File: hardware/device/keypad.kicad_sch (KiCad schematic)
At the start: 55 parts, among them SW1 TRIG1, SW10 TRIG10, SW11 TRIG11, SW12 TRIG12, SW13 TRIG13, SW14 TRIG14, SW15 TRIG15, SW16 TRIG16, SW17 WHEEL_BTN, SW18 HELP, SW19 LEFT_BTN, SW2 TRIG2, SW20 RIGHT_BTN, SW3 TRIG3, SW4 TRIG4, SW5 TRIG5, SW6 TRIG6, SW7 TRIG7, SW8 TRIG8, SW9 TRIG9, U10 TRIG9, U11 TRIG13, U12 TRIG10, U13 TRIG14, U14 TRIG11, U15 TRIG15, U16 TRIG12, U17 TRIG16, U2 TRIG1, U25 TCA8418RTWR, U3 TRIG2, U4 TRIG3, U5 TRIG4, U6 TRIG8, U7 TRIG7, U8 TRIG6, U9 TRIG5

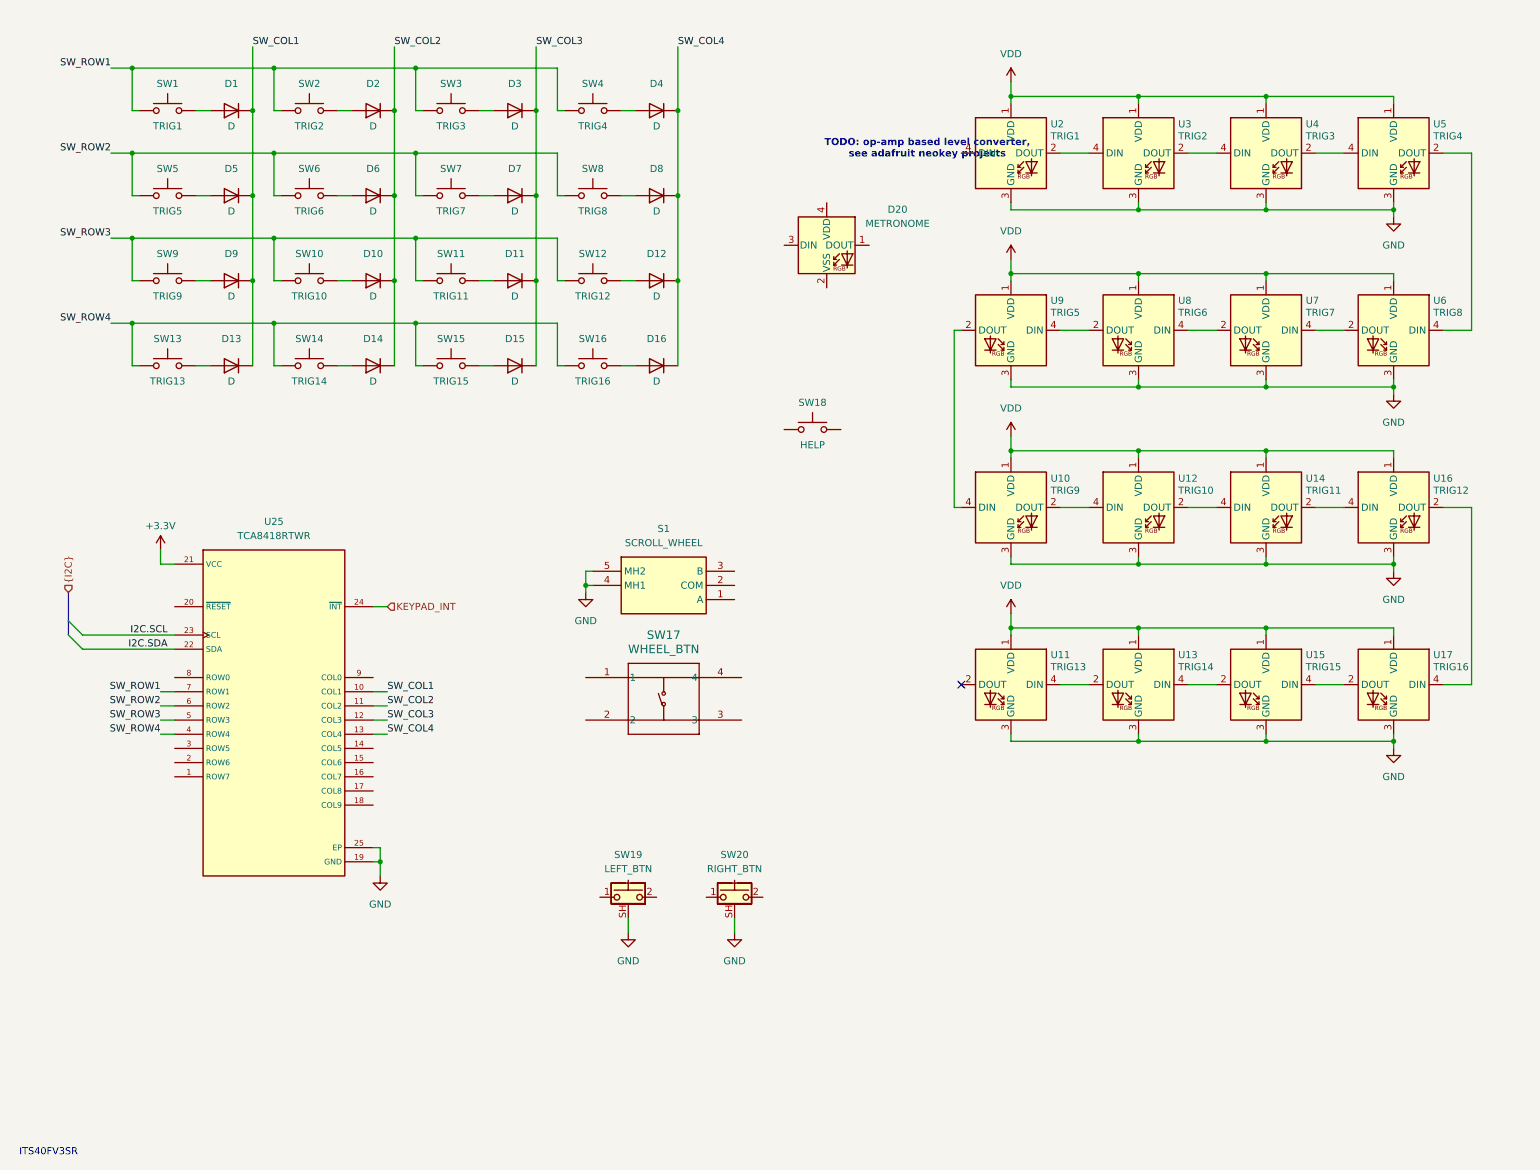
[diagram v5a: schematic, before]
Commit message: feat: various layout, start adding capacitive pads
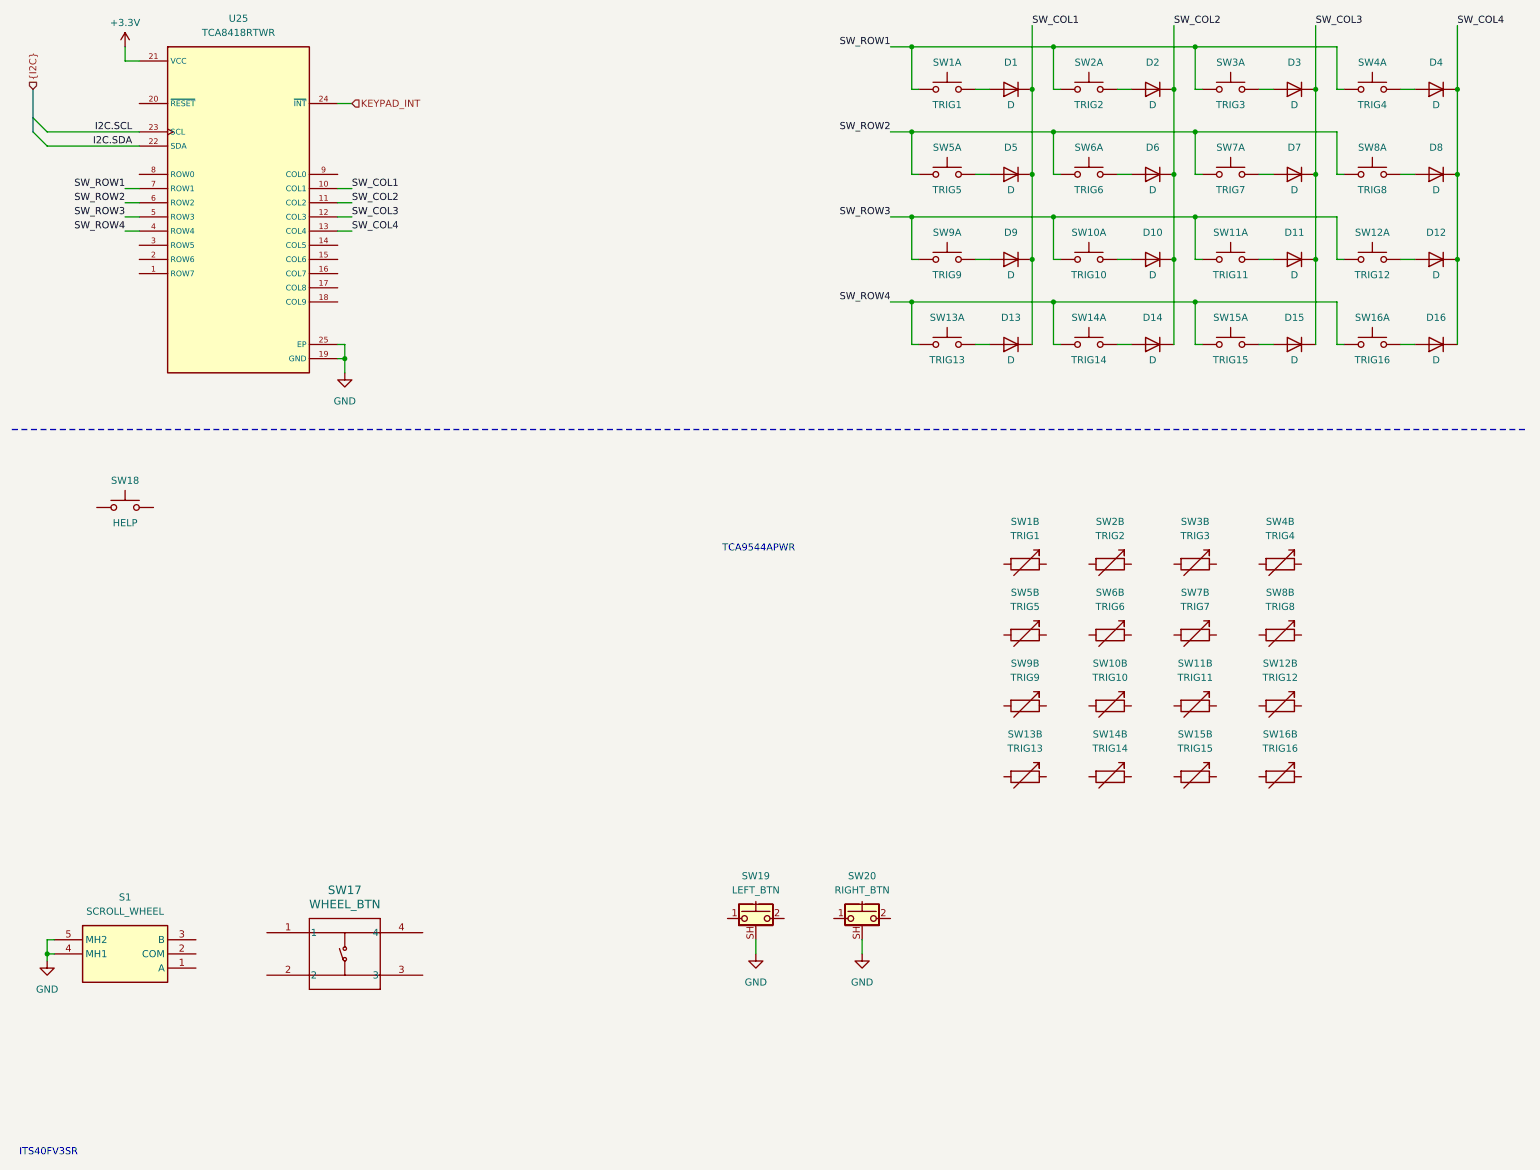
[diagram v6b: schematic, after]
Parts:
- removed D20: METRONOME, LED_SMD:LED_SK6812MINI_PLCC4_3.5x3.5mm_P1.75mm, symbol LED:SK6812MINI
- removed U10: TRIG9, pocket_synth:SK6812MINI-E, symbol pocket_synth:SK6812MINI-E
- removed U11: TRIG13, pocket_synth:SK6812MINI-E, symbol pocket_synth:SK6812MINI-E
- removed U12: TRIG10, pocket_synth:SK6812MINI-E, symbol pocket_synth:SK6812MINI-E
- removed U13: TRIG14, pocket_synth:SK6812MINI-E, symbol pocket_synth:SK6812MINI-E
- removed U14: TRIG11, pocket_synth:SK6812MINI-E, symbol pocket_synth:SK6812MINI-E
- removed U15: TRIG15, pocket_synth:SK6812MINI-E, symbol pocket_synth:SK6812MINI-E
- removed U16: TRIG12, pocket_synth:SK6812MINI-E, symbol pocket_synth:SK6812MINI-E
- removed U17: TRIG16, pocket_synth:SK6812MINI-E, symbol pocket_synth:SK6812MINI-E
- removed U2: TRIG1, pocket_synth:SK6812MINI-E, symbol pocket_synth:SK6812MINI-E
- removed U3: TRIG2, pocket_synth:SK6812MINI-E, symbol pocket_synth:SK6812MINI-E
- removed U4: TRIG3, pocket_synth:SK6812MINI-E, symbol pocket_synth:SK6812MINI-E
- removed U5: TRIG4, pocket_synth:SK6812MINI-E, symbol pocket_synth:SK6812MINI-E
- removed U6: TRIG8, pocket_synth:SK6812MINI-E, symbol pocket_synth:SK6812MINI-E
- removed U7: TRIG7, pocket_synth:SK6812MINI-E, symbol pocket_synth:SK6812MINI-E
- removed U8: TRIG6, pocket_synth:SK6812MINI-E, symbol pocket_synth:SK6812MINI-E
- removed U9: TRIG5, pocket_synth:SK6812MINI-E, symbol pocket_synth:SK6812MINI-E
- SW1, SW10, SW11, SW12, SW13, SW14, SW15, SW2, SW3, SW4, SW5, SW6, SW7, SW8, SW9: symbol Switch:SW_Push -> pocket_synth:SW_Push_Pressure
- SW16: footprint pocket_synth:SW_Hotswap_Kailh_Choc_V1V2_Plated_1.00u -> pocket_synth:SW_Hotswap_Kailh_Choc_V1_1.00u_Pressure; symbol Switch:SW_Push -> pocket_synth:SW_Push_Pressure
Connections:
- no-connect marks 1 -> 0
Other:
- note added: "TCA9544APWR"
- note removed: "TODO: op-amp based level converter, see adafruit neokey projects"
- moved on the sheet: D1, D10, D11, D12, D13, D14, D15, D16, D2, D3, D4, D5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

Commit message: feat: add integrated flash memory
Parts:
- added unit 2 of SW1
- added unit 2 of SW10
- added unit 2 of SW11
- added unit 2 of SW12
- added unit 2 of SW13
- added unit 2 of SW14
- added unit 2 of SW15
- added unit 2 of SW16
- added unit 2 of SW2
- added unit 2 of SW3
- added unit 2 of SW4
- added unit 2 of SW5
- added unit 2 of SW6
- added unit 2 of SW7
- added unit 2 of SW8
- added unit 2 of SW9

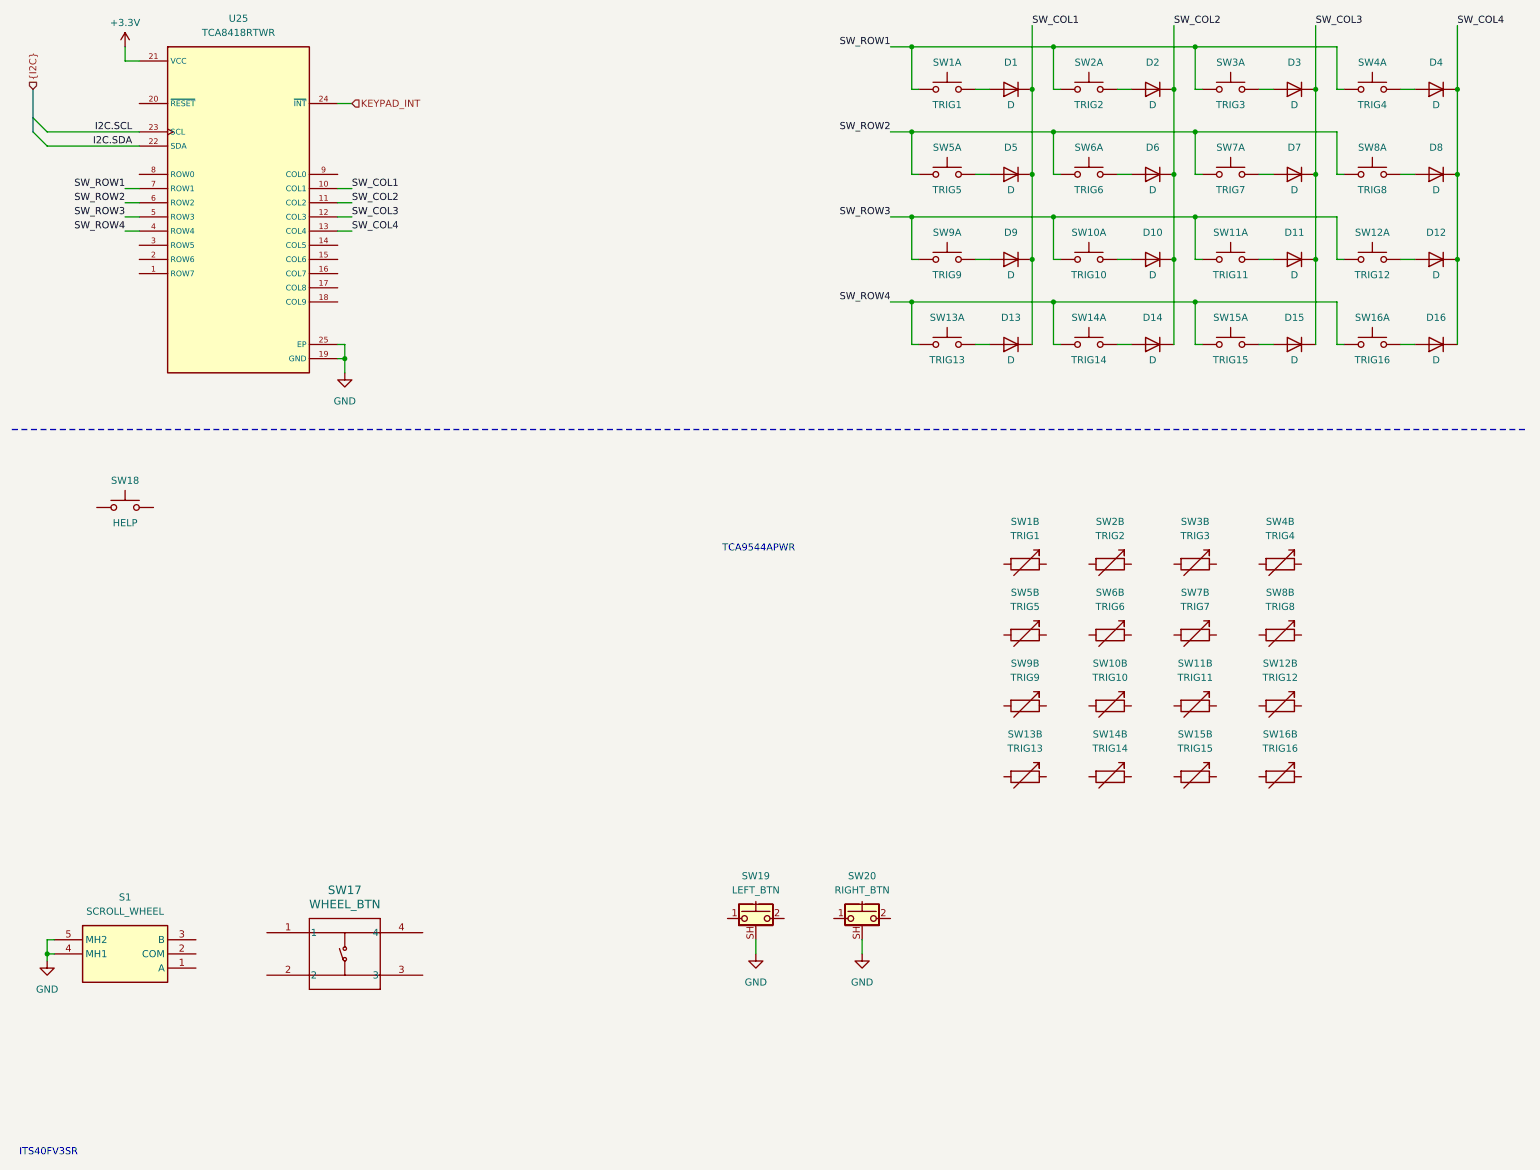
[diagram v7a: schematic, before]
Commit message: feat: start adding velocity button circuit
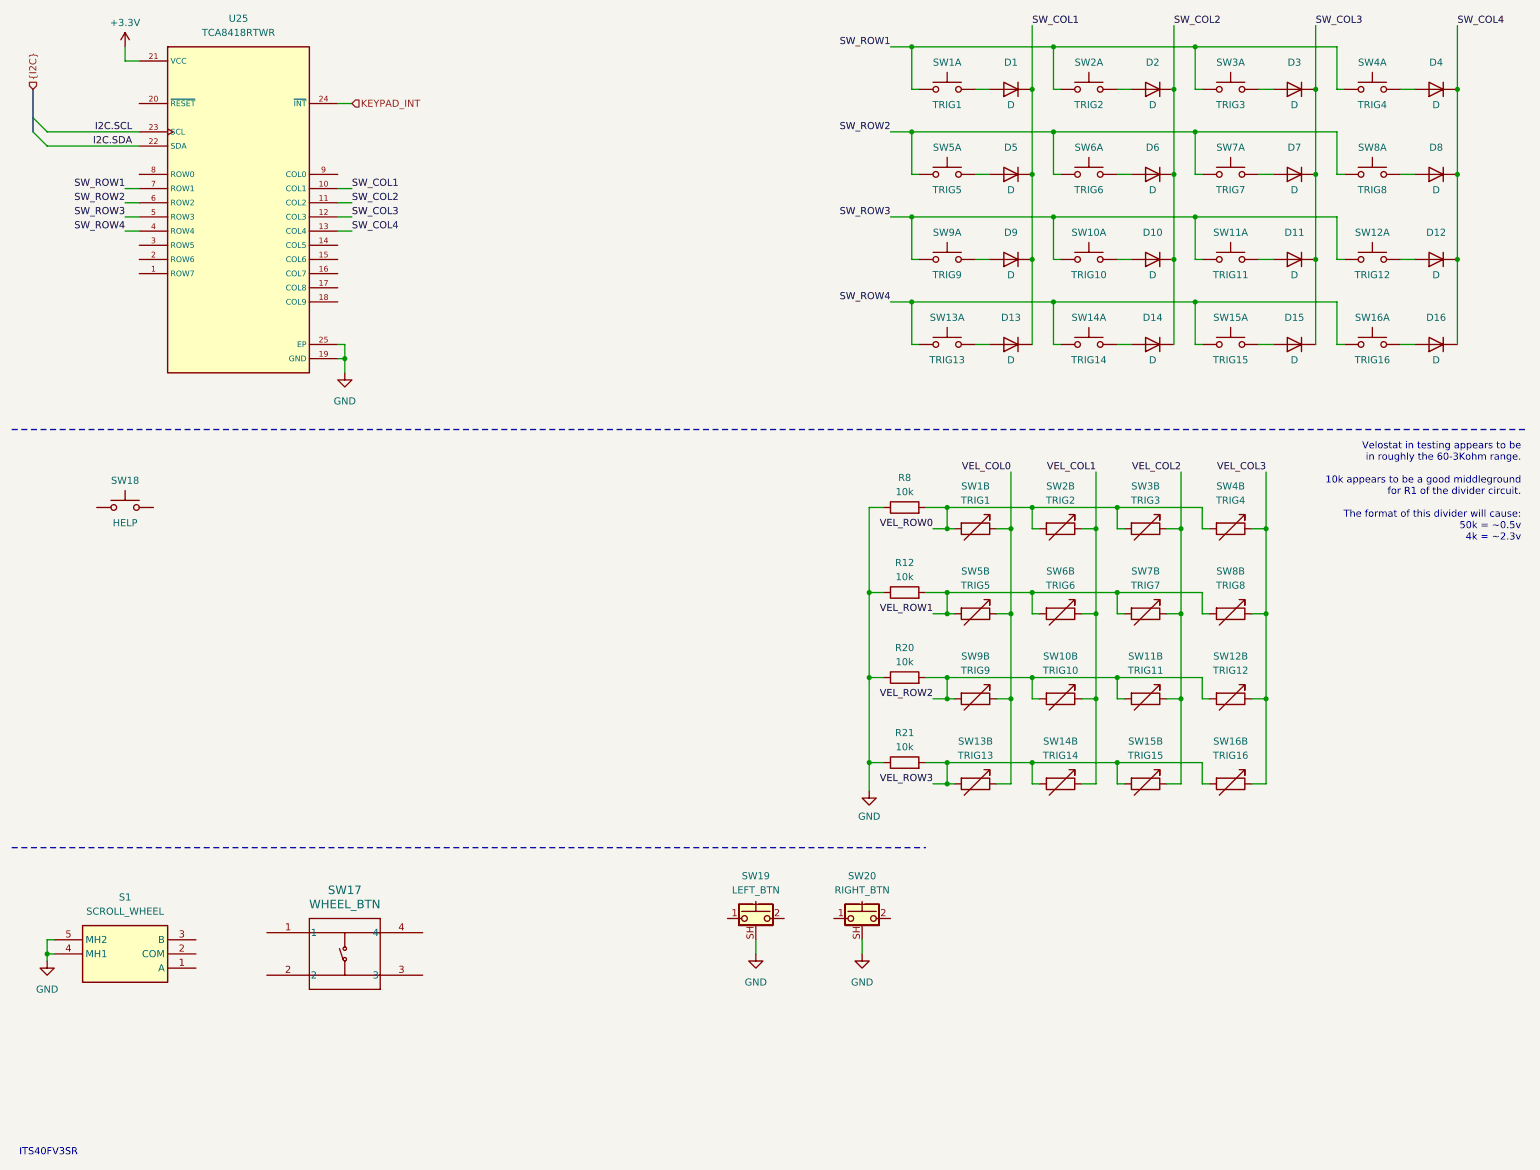
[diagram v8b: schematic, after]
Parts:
- added R12, R20, R21, R8: 10k, symbol Device:R
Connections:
- net GND: now also R12.1, R20.1, R21.1, R8.1
- net VEL_ROW1: now reaches SW6.3
- net VEL_ROW1: now also SW5.3, SW7.3, SW8.3, R12.2
- net VEL_COL1: now reaches SW6.4
- net VEL_COL1: now also SW10.4, SW14.4, SW2.4
- net VEL_ROW3: now reaches SW13.3
- net VEL_ROW3: now also SW14.3, SW15.3, SW16.3, R21.2
- net VEL_COL0: now reaches SW13.4
- net VEL_COL0: now also SW1.4, SW5.4, SW9.4
- net VEL_ROW2: now reaches SW11.3
- net VEL_ROW2: now also SW10.3, SW12.3, SW9.3, R20.2
- net VEL_COL2: now reaches SW11.4
- net VEL_COL2: now also SW15.4, SW3.4, SW7.4
- net VEL_ROW0: now reaches SW4.3
- net VEL_ROW0: now also SW1.3, SW2.3, SW3.3, R8.2
- net VEL_COL3: now reaches SW4.4
- net VEL_COL3: now also SW12.4, SW16.4, SW8.4
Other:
- note added: "Velostat in testing appears to be in roughly the 60-3Kohm range. 10k appears to be a good middleground for R1 of the divider circuit. The format of this divider will cause: 50k = ~0.5v 4k = ~2.3v"
- note removed: "TCA9544APWR"
- moved on the sheet: SW10B, SW11B, SW12B, SW13B, SW14B, SW15B, SW16B, SW1B, SW2B, SW3B, SW4B, SW5B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
